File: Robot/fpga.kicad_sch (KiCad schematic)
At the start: 45 parts, among them J12 M1, J13 M2, J14 M3, J15 M4, SW1 User, U3 DRV8845RHHR, U4 ICE40UP5K-SG48ITR, U5 74HCT245, U6 MCP4728

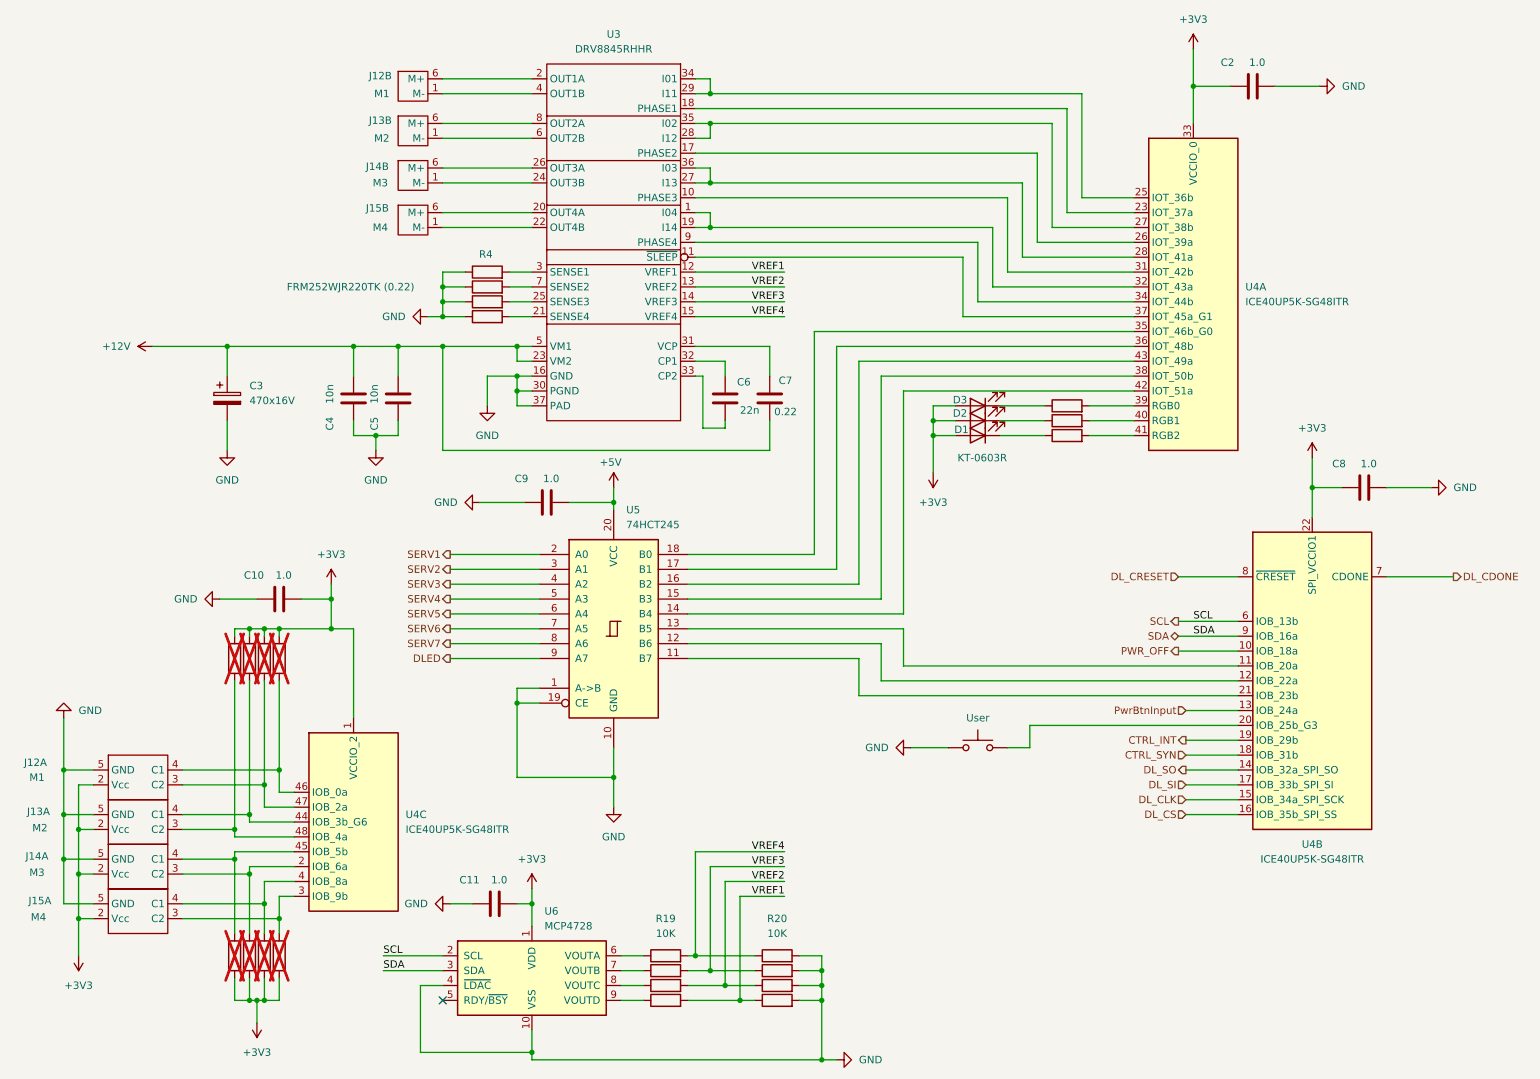
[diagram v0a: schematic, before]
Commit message: Updated PCB for Robot (routing finished, postprocessing in progress)
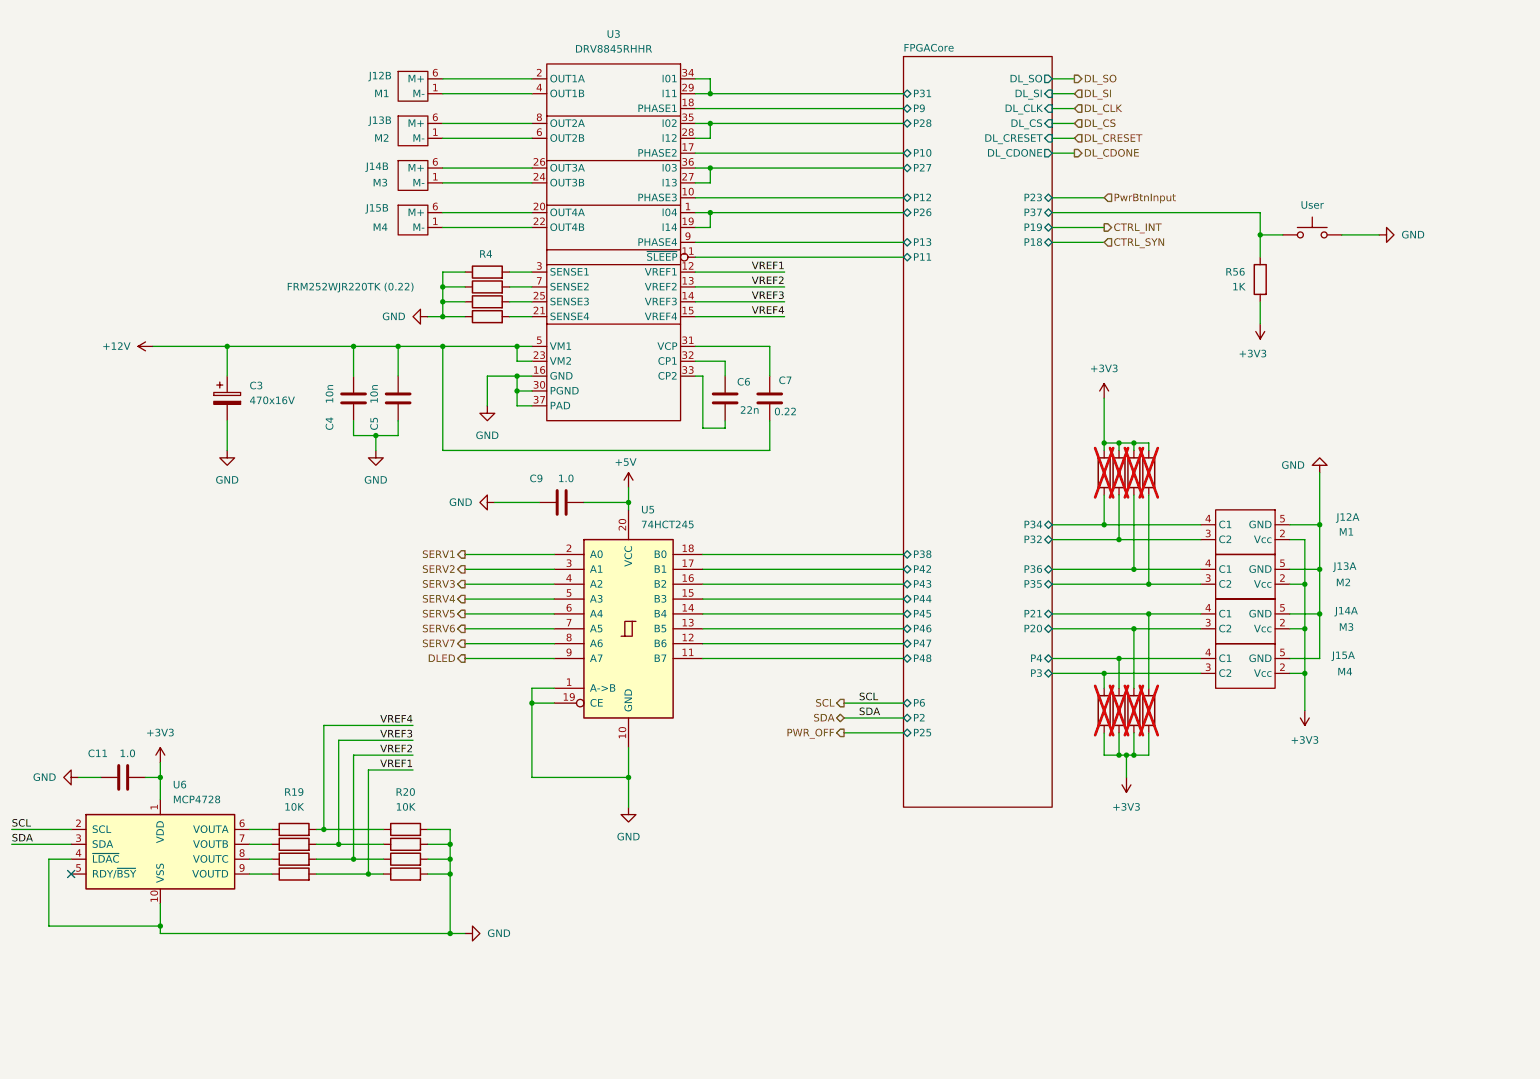
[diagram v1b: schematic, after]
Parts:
- removed C10, C2, C8: 1.0, Capacitor_SMD:C_0603_1608Metric_Pad1.08x0.95mm_HandSolder, symbol Device:C
- removed D1, D2, D3: KT-0603R, LED_SMD:LED_0603_1608Metric, symbol Device:LED
- removed R10, R8, R9: ~, Resistor_SMD:R_0603_1608Metric_Pad0.98x0.95mm_HandSolder, symbol Device:R
- removed U4: ICE40UP5K-SG48ITR, Package_DFN_QFN:QFN-48-1EP_7x7mm_P0.5mm_EP5.6x5.6mm, symbol FPGA_Lattice:ICE40UP5K-SG48ITR
- added R56: 1K, Resistor_SMD:R_0603_1608Metric_Pad0.98x0.95mm_HandSolder, symbol Device:R
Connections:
- net +3V3: now also R56.2
- net FPGACore/P34: now reaches J12.4 (C1), R14.1
- net FPGACore/P3: now reaches J15.3 (C2), R18.1
- net FPGACore/P4: now reaches J15.4 (C1), R17.1
- net FPGACore/P37: now reaches SW1.2
- net FPGACore/P37: now also R56.1
- net FPGACore/P20: now reaches J14.3 (C2), R16.1
- net FPGACore/P21: now reaches J14.4 (C1), R15.1
- net FPGACore/P35: now reaches J13.3 (C2), R11.1
- net FPGACore/P36: now reaches J13.4 (C1), R12.1
- net FPGACore/P9: now reaches U3.18 (PHASE1)
- net FPGACore/P31: now reaches U3.29 (I11), U3.34 (I01)
- net FPGACore/P10: now reaches U3.17 (PHASE2)
- net FPGACore/P28: now reaches U3.28 (I12), U3.35 (I02)
- net FPGACore/P27: now reaches U3.27 (I13), U3.36 (I03)
- net FPGACore/P12: now reaches U3.10 (PHASE3)
- net FPGACore/P26: now reaches U3.1 (I04), U3.19 (I14)
- net FPGACore/P13: now reaches U3.9 (PHASE4)
- net FPGACore/P38: now reaches U5.18 (B0)
- net FPGACore/P42: now reaches U5.17 (B1)
- net FPGACore/P11: now reaches U3.11 (~{SLEEP})
- net FPGACore/P44: now reaches U5.15 (B3)
- net FPGACore/P45: now reaches U5.14 (B4)
- net FPGACore/P43: now reaches U5.16 (B2)
- net FPGACore/P32: now reaches J12.3 (C2), R13.1
- net FPGACore/P46: now reaches U5.13 (B5)
- net FPGACore/P47: now reaches U5.12 (B6)
- net FPGACore/P48: now reaches U5.11 (B7)
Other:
- added sheet FPGACore (fpga_core.kicad_sch)
- moved on the sheet: C11, C9, J12A, J13A, J14A, J15A, R19, R20, U5, U6

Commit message: Added LCSC PN for all PCBA components
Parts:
- U3: MPN (none) -> C20345375
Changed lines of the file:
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@@
+			)
+		)
+		(property "MPN" "C20345375"
+			(at 124.46 53.34 0)
+			(effects
+				(font
+					(size 1.27 1.27)
+				)
+				(hide yes)
 			)
 		)
